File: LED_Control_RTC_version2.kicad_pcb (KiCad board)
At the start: 4 copper layers, 100 x 80 mm, 140 parts, among them J1 Conn_02x04_Odd_Even, J101 Conn_01x06_Male, J102 Conn_01x06_Male, J2 DS1023-2*8SF11, J20 DS1023-2*8SF11, J200 Conn_ARM_JTAG_SWD_10, J3 Screw_Terminal_01x02, J4 Conn_ARM_JTAG_SWD_10, J5 Conn_01x03_Female, J6 Conn_01x02, Q1 IRLR8726TRPBF, Q10 IRLR8726TRPBF, Q11 PJM2309PSA, Q2 IRLR8726TRPBF, Q3 IRLR8726TRPBF, Q4 IRLR8726TRPBF, Q5 IRLR8726TRPBF, Q6 IRLR8726TRPBF, Q7 IRLR8726TRPBF, Q8 IRLR8726TRPBF, Q9 IRLR8726TRPBF, U1 STM32F103C8Tx, U10 AT24C16D-XHM-B, U101 TC4427, U102 TC4427, U103 TC4427, U104 TC4427, U105 TC4427, U2 STM32G030C6Tx, U3 MAX3485, U5 TPS5401, U6 LM1117-3.3, Y1 16MHz, Y2 32.768KHz

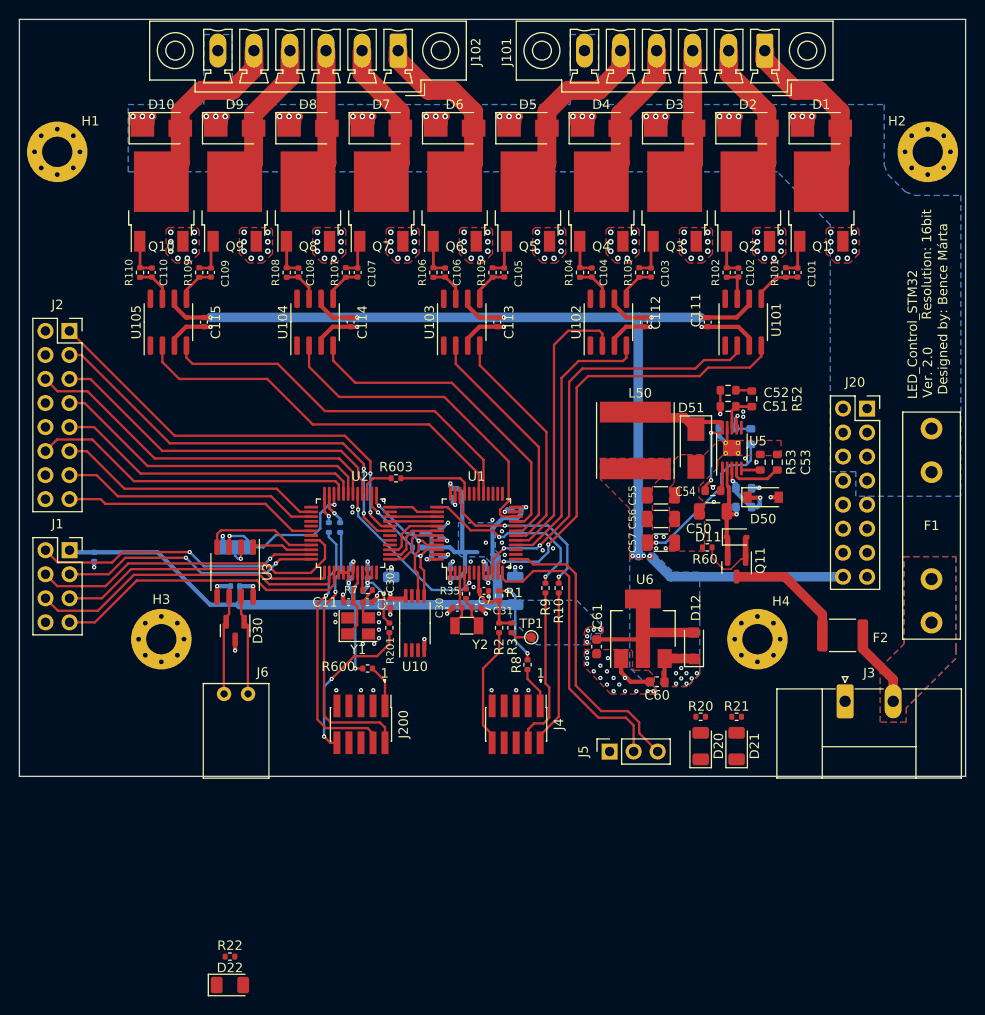
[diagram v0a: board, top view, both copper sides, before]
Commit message: Cleaned up messy reference numbering Added labels to schematic
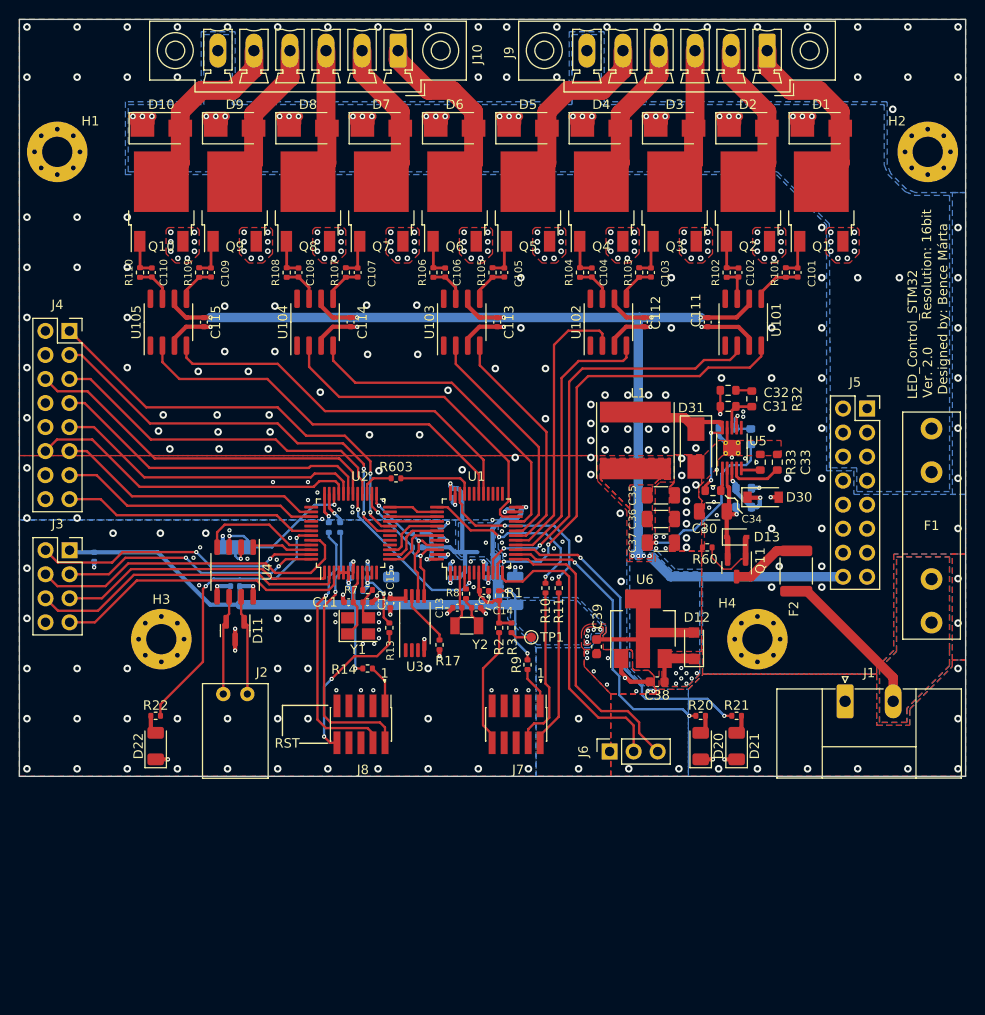
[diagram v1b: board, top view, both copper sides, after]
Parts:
- added R17: 10k, Resistor_SMD:R_0402_1005Metric, F.Cu at (139.4, 121.1)
- C32: renamed from C52; value 6n8 -> 2n7
- moved R22 26.6 mm to (109.4, 128.6)
- moved D22 26.4 mm to (109.4, 131.8), turned to 90 degrees
- moved F2 8.38 mm to (177.1, 113.3), turned to 90 degrees
- moved J9 0.25 mm to (174.0, 58.3)
- moved R20 0.10 mm to (167.0, 128.6)
- moved R21 0.10 mm to (170.8, 128.6)
- moved J2 0.08 mm to (116.5, 126.3)
- renumbered C200 to C10, C30 to C13, C31 to C14, C301 to C15, C9 to C16, C50 to C30, C51 to C31, C53 to C33, C54 to C34, C55 to C35, C56 to C36, C57 to C37, C60 to C38, C61 to C39, C10 to C501, C300 to C9, D30 to D11, D11 to D13, D50 to D30, D51 to D31, J3 to J1, J102 to J10, J6 to J2, J1 to J3, J2 to J4, J20 to J5, J5 to J6, J4 to J7, J200 to J8, J101 to J9, L50 to L1, R9 to R10, R10 to R11, R200 to R12, R201 to R13, R600 to R14, R601 to R15, R602 to R16, R50 to R30, R51 to R31, R52 to R32, R53 to R33, R54 to R34, R55 to R35, R35 to R8, R8 to R9, U10 to U3, U3 to U4
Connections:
- U1 pad 14: unconnected-(U1-Pad14) -> /MCUs + Peripherals/LED1
- U1 pad 15: unconnected-(U1-Pad15) -> /MCUs + Peripherals/LED2
- U2 pad 43: unconnected-(U2-Pad43) -> /MCUs + Peripherals/LED3
- U3 pad 7: unconnected-(U10-Pad7) -> Net-(U3-Pad7)
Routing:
- net /MCUs + Peripherals/LED2: track 0.00 -> 34.8 mm, vias 0 -> 2
- net /MCUs + Peripherals/LED1: track 0.00 -> 31.6 mm, vias 0 -> 2
- net /MCUs + Peripherals/LED3: track 0.00 -> 30.3 mm, vias 0 -> 2
- net /Power Delivery/Power_IN: track 8.30 -> 16.5 mm
- net Net-(F2-Pad2): track 13.1 -> 7.13 mm
- net Net-(U3-Pad7): track 0.00 -> 5.86 mm
- net GND: track 66.6 -> 71.4 mm, vias 164 -> 361
- net Net-(D22-Pad2): track 0.00 -> 2.01 mm
- net Net-(D21-Pad2): track 0.00 -> 1.91 mm
- net Net-(D20-Pad2): track 0.00 -> 1.91 mm
- net +5V: track 147.5 -> 148.5 mm
- net /MCUs + Peripherals/M2_USART1_DE: track 17.2 -> 16.3 mm
- net /MCUs + Peripherals/M2_USART1_TX: track 12.1 -> 12.7 mm
- net /MCUs + Peripherals/M1_SWDIO: track 19.1 -> 19.6 mm
- added copper zone on B.Cu, net GND
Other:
- board text added: "RST"

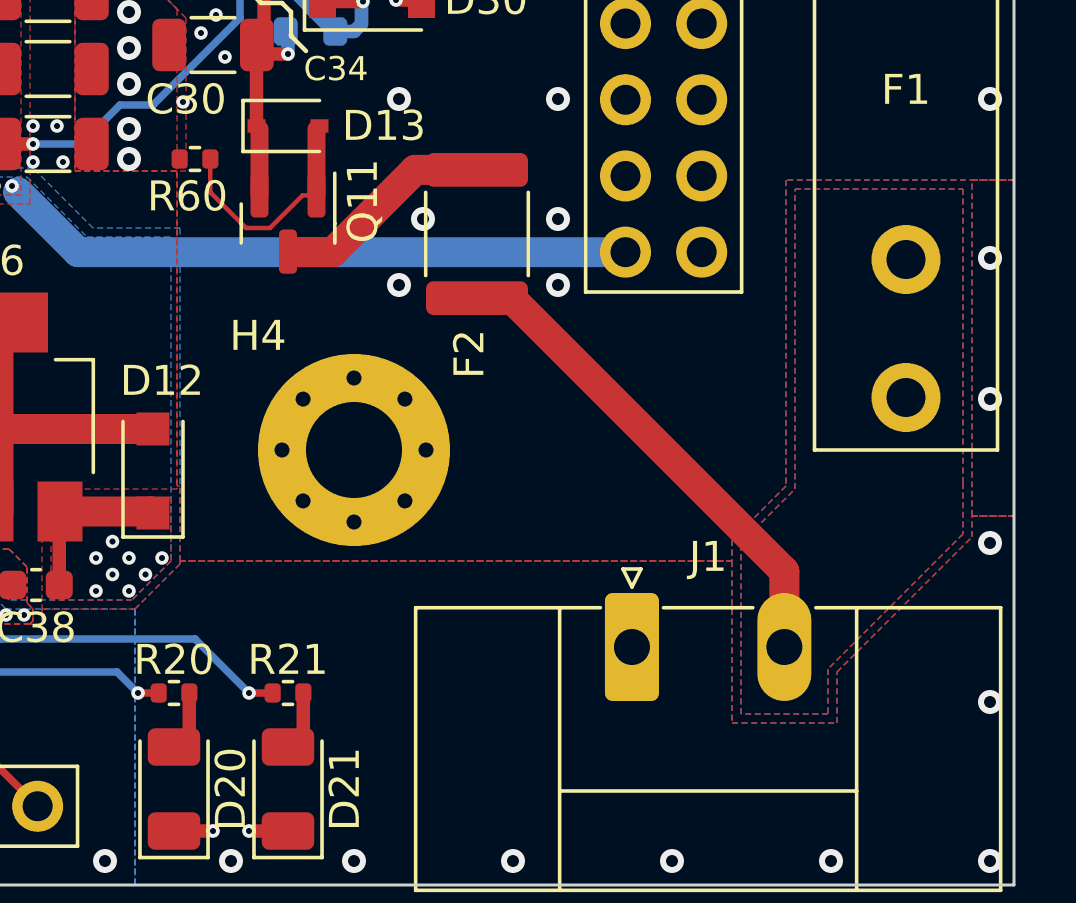
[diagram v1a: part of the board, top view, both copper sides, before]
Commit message: Added TVS diode on power input
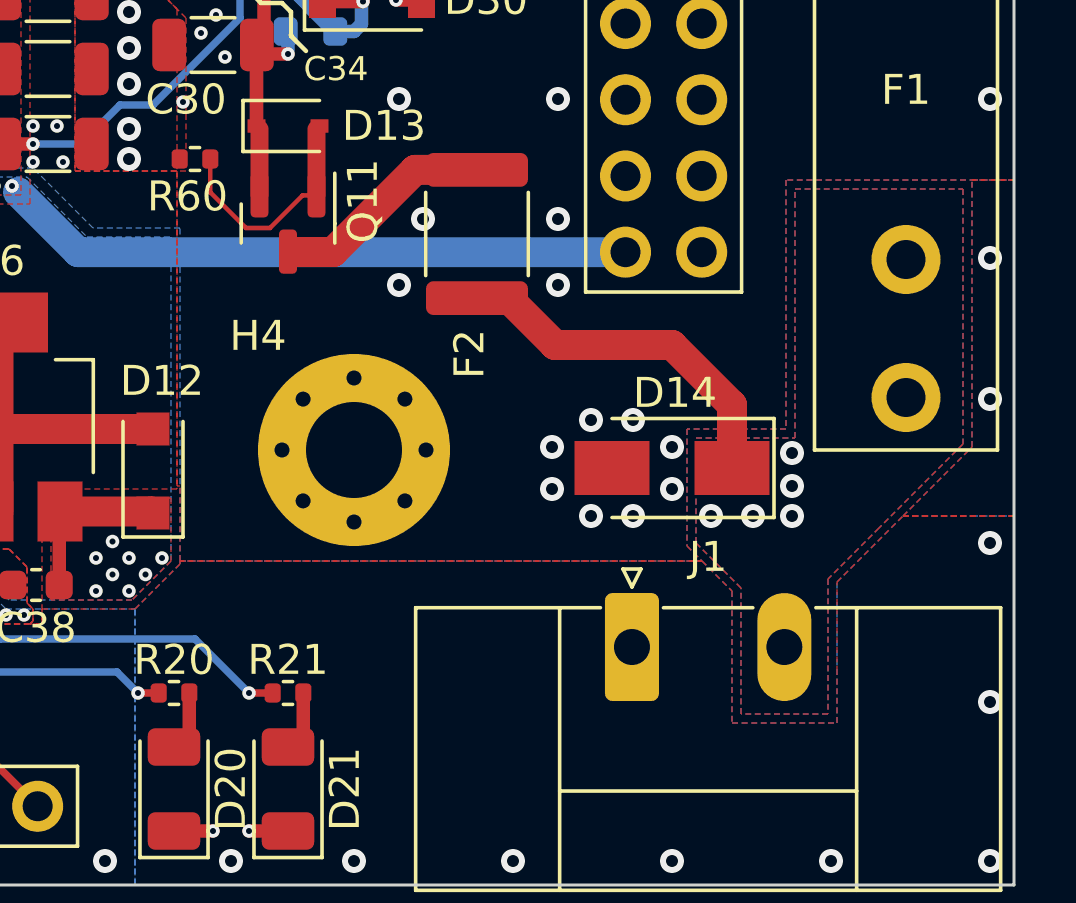
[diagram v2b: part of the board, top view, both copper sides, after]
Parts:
- added D14: SMAJ26A, Diode_SMD:D_SMA, F.Cu at (183.6, 121.1)
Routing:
- net /Power Delivery/Power_IN: track 16.5 -> 12.1 mm, vias 0 -> 5
- net GND: vias 361 -> 369
